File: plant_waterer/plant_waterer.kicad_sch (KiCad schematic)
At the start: 16 parts, among them J1 PJ-002AH, J2 Conn_01x02, J3 Conn_01x03, U1 XIAO_RP2040, U2 TB6612FNG,C,8,EL, U3 OLED_DISP, U4 AP2204R-5.0TRG1

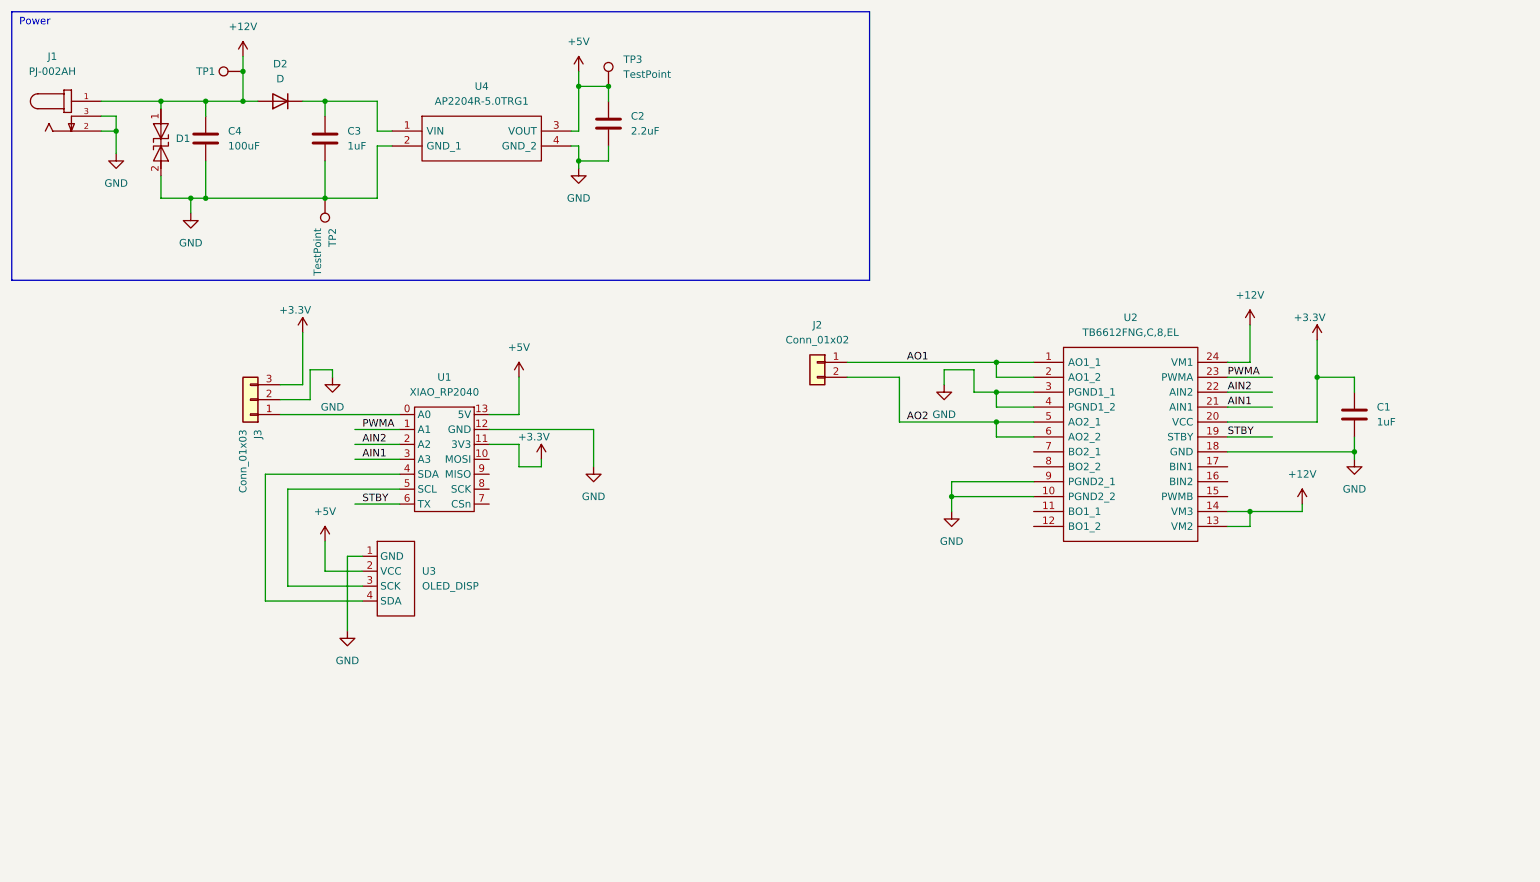
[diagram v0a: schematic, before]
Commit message: Added UART input Added second motor output Added fuse and reverse polarity protection
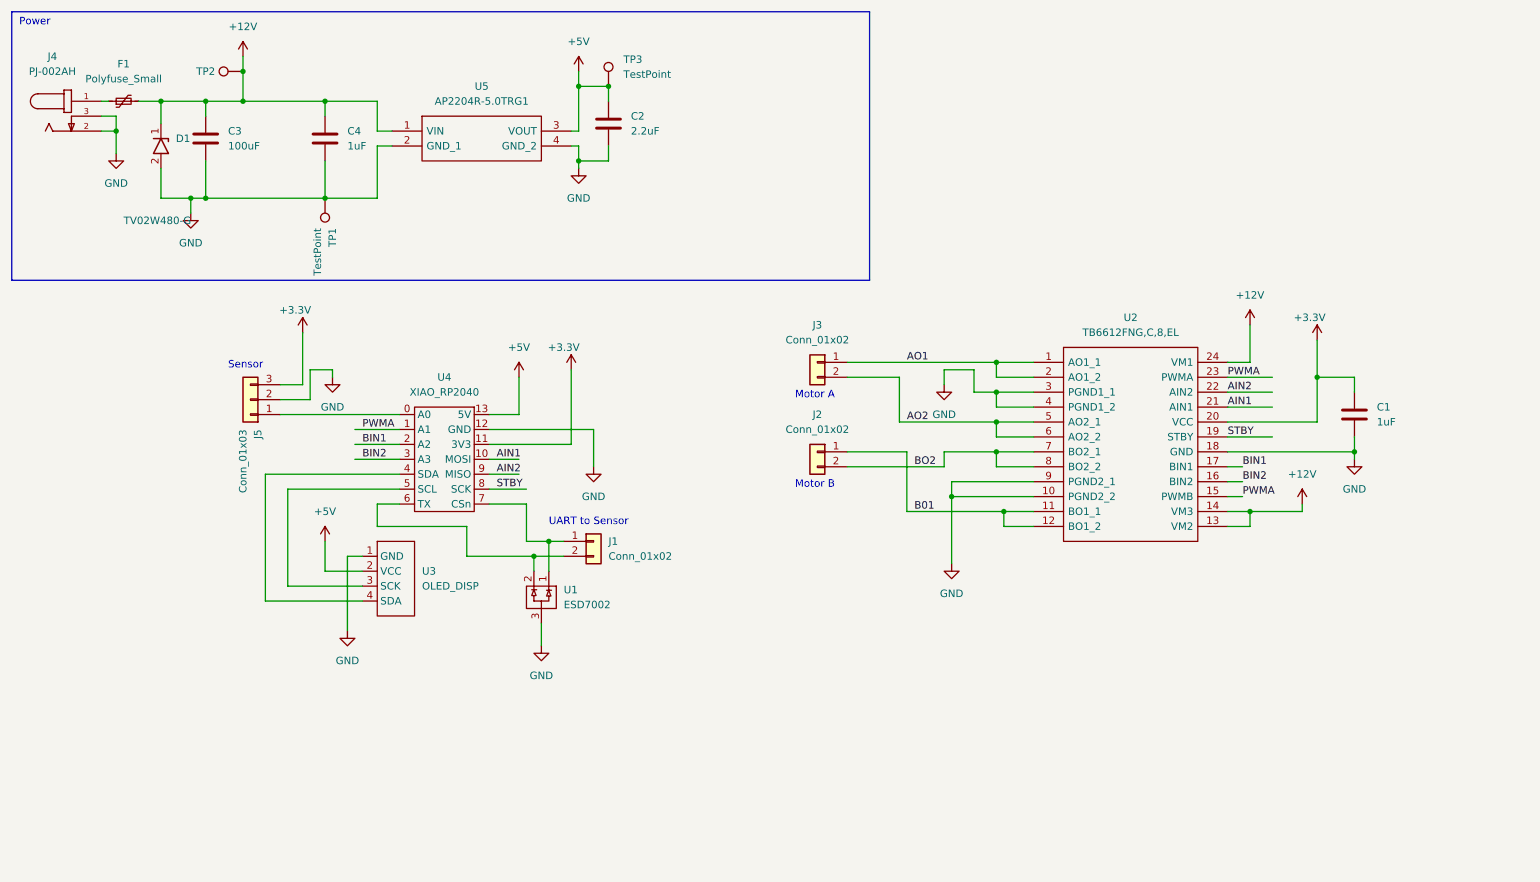
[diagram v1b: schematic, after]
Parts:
- removed D1: SP3130-01ETG, Library:SP3130-01ETG, symbol MySymbols:SP3130-01ETG
- removed D2: D, Diode_SMD:D_SOD-123, symbol Device:D
- added D1: TV02W480-G, Diode_SMD:D_SOD-123, symbol MySymbols:TV02W480-G
- added F1: Polyfuse_Small, Fuse:Fuse_1210_3225Metric_Pad1.42x2.65mm_HandSolder, symbol Device:Polyfuse_Small
- added J1: Conn_01x02, Connector_PinHeader_2.54mm:PinHeader_1x02_P2.54mm_Vertical, symbol Connector_Generic:Conn_01x02
- added J2: Conn_01x02, Library:CONN 1x2 5mm, symbol Connector_Generic:Conn_01x02
- added U1: ESD7002, Package_TO_SOT_SMD:SOT-323_SC-70_Handsoldering, symbol MySymbols:ESD7002
- TP1: renamed from TP2; footprint TestPoint:TestPoint_2Pads_Pitch2.54mm_Drill0.8mm -> TestPoint:TestPoint_Loop_D1.80mm_Drill1.0mm_Beaded
- TP2: renamed from TP1; footprint TestPoint:TestPoint_Pad_1.5x1.5mm -> TestPoint:TestPoint_Loop_D1.80mm_Drill1.0mm_Beaded
- TP3: footprint TestPoint:TestPoint_Pad_1.5x1.5mm -> TestPoint:TestPoint_Loop_D1.80mm_Drill1.0mm_Beaded
- renumbered C4 to C3, C3 to C4, J2 to J3, J1 to J4, J3 to J5, U1 to U4, U4 to U5
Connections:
- net +12V: now also C4.2, U5.1 (VIN), D1.1, F1.2; no longer J4.1
- net AIN1: now also U4.10 (MOSI); no longer U4.3 (A3)
- net AIN2: now also U4.9 (MISO); no longer U4.2 (A2)
- net GND: now also D1.2, U1.3
- net PWMA: now also U2.15 (PWMB)
- net STBY: now also U4.8 (SCK); no longer U4.6 (TX)
- net B01: now reaches U2.11 (BO1_1)
- net B01: now also U2.12 (BO1_2), J2.1 (Pin_1)
- net BIN2: now reaches U2.16 (BIN2)
- net BIN2: now also U4.3 (A3)
- net BIN1: now reaches U2.17 (BIN1)
- net BIN1: now also U4.2 (A2)
- net BO2: now reaches U2.7 (BO2_1)
- net BO2: now also U2.8 (BO2_2), J2.2 (Pin_2)
- net at U4.7 (CSn): now also J1.1 (Pin_1), U1.1
- new net: J1.2 (Pin_2), U1.2, U4.6 (TX)
- new net: F1.1, J4.1
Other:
- note added: "Motor A"
- note added: "Motor B"
- note added: "Sensor"
- note added: "UART to Sensor"

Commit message: Add adjustable level set Add power filtering Add ESD
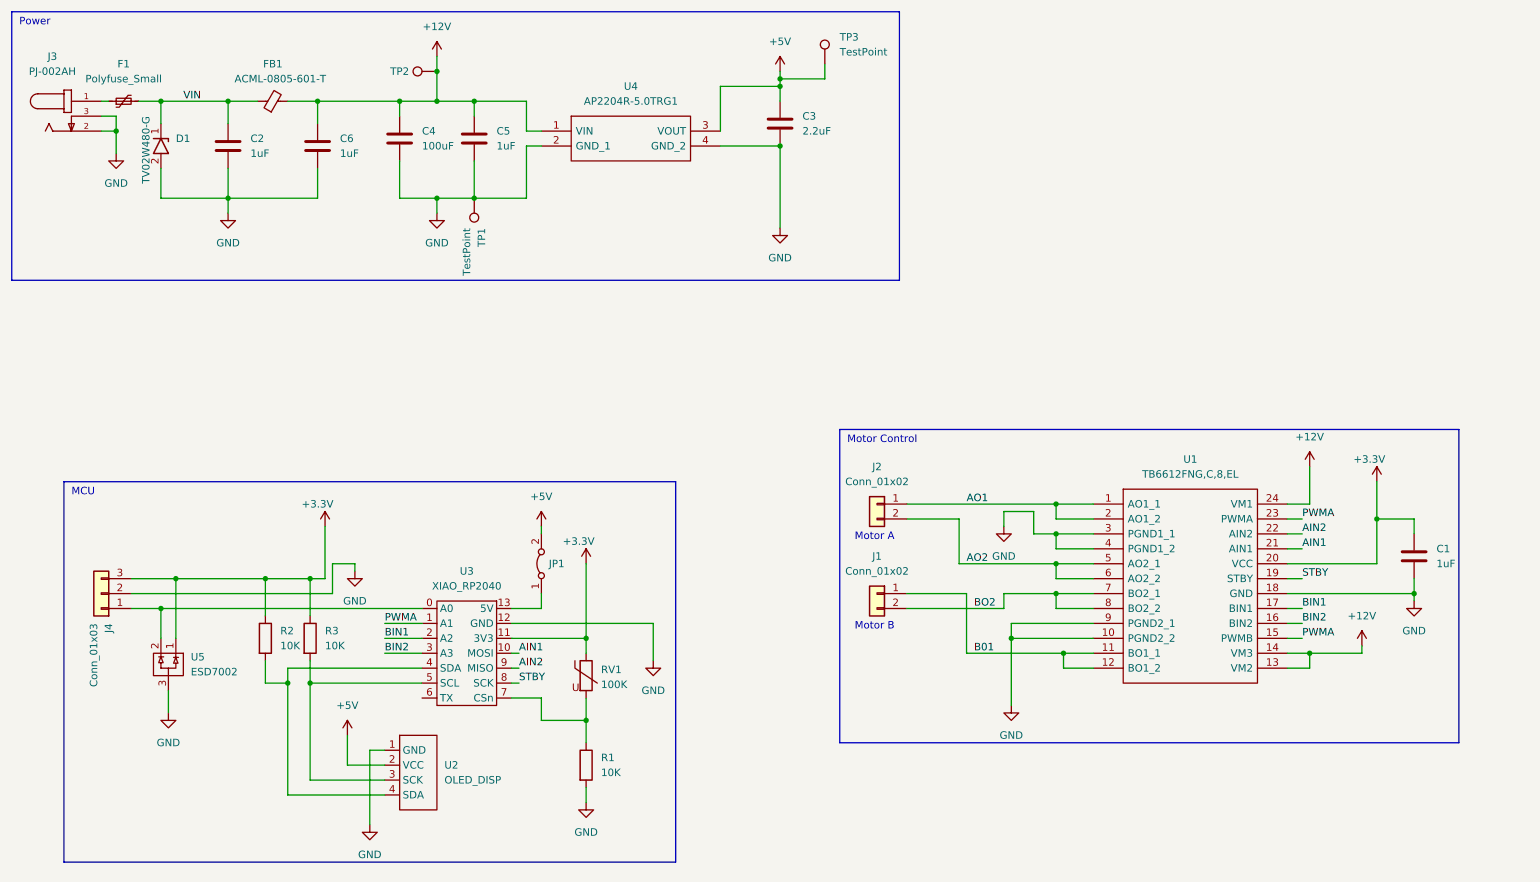
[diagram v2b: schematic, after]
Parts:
- removed J1: Conn_01x02, Connector_PinHeader_2.54mm:PinHeader_1x02_P2.54mm_Vertical, symbol Connector_Generic:Conn_01x02
- removed U1: ESD7002, Package_TO_SOT_SMD:SOT-323_SC-70_Handsoldering, symbol MySymbols:ESD7002
- added C2, C6: 1uF, Capacitor_SMD:C_0805_2012Metric_Pad1.18x1.45mm_HandSolder, symbol Device:C
- added FB1: ACML-0805-601-T, Resistor_SMD:R_0805_2012Metric_Pad1.20x1.40mm_HandSolder, symbol Device:FerriteBead_Small
- added JP1: Jumper_2_Bridged, Connector_PinHeader_2.54mm:PinHeader_1x02_P2.54mm_Vertical, symbol Jumper:Jumper_2_Bridged
- added R1, R2, R3: 10K, Resistor_SMD:R_0805_2012Metric_Pad1.20x1.40mm_HandSolder, symbol Device:R
- added RV1: 100K, Connector_PinHeader_2.54mm:PinHeader_1x03_P2.54mm_Vertical, symbol Device:Varistor
- added U5: ESD7002, Package_TO_SOT_SMD:SOT-323_SC-70_Handsoldering, symbol MySymbols:ESD7002
- renumbered C2 to C3, C3 to C4, C4 to C5, J2 to J1, J3 to J2, J4 to J3, J5 to J4, U2 to U1, U3 to U2, U4 to U3, U5 to U4
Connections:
- net +12V: now also C6.2, FB1.2; no longer D1.1, F1.2
- net +3.3V: now also R2.1, R3.1, RV1.1, U5.1
- net +5V: now also JP1.2 (B); no longer U3.13 (5V)
- net GND: now also C2.1, C6.1, R1.2, U5.3
- net at U3.7 (CSn): now also R1.1, RV1.2
- net at J4.1 (Pin_1), U3.0 (A0): now also U5.2
- net at U2.4 (SDA), U3.4 (SDA): now also R2.2
- net at U2.3 (SCK), U3.5 (SCL): now also R3.2
- new net: JP1.1 (A), U3.13 (5V)
- new net VIN: C2.2, D1.1, F1.2, FB1.1
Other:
- note added: "MCU"
- note added: "Motor Control"
- note removed: "Sensor"
- note removed: "UART to Sensor"
- moved on the sheet: C1, C3, C4, C5, J1, J2, J4, TP1, TP2, TP3, U1, U2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

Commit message: Minor clean up and adding schmatic
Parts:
- renumbered C3 to C2, C2 to C3, U5 to U4, U4 to U5
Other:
- moved on the sheet: TP3
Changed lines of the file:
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@@
   (junction (at 256.54 115.57) (diameter 0) (color 0 0 0 0)
   )
-  (junction (at 148.59 27.94) (diameter 0) (color 0 0 0 0)
-  )
   (junction (at 195.58 115.57) (diameter 0) (color 0 0 0 0)
   )
@@
   (junction (at 54.61 48.26) (diameter 0) (color 0 0 0 0)
   )
+  (junction (at 138.43 29.21) (diameter 0) (color 0 0 0 0)
+  )
   (junction (at 64.77 130.81) (diameter 0) (color 0 0 0 0)
   )
@@
     (stroke (width 0) (type default) (color 0 0 0 0))
   )
-  (polyline (pts (xy 168.91 62.23) (xy 17.78 62.23))
+  (polyline (pts (xy 160.02 62.23) (xy 17.78 62.23))
     (stroke (width 0) (type default) (color 0 0 0 0))
   )
@@
     (stroke (width 0) (type default) (color 0 0 0 0))
   )
-  (wire (pts (xy 148.59 26.67) (xy 148.59 27.94))
-    (stroke (width 0) (type default) (color 0 0 0 0))
-  )
   (wire (pts (xy 105.41 36.83) (xy 107.95 36.83))
     (stroke (width 0) (type default) (color 0 0 0 0))
@@
     (stroke (width 0) (type default) (color 0 0 0 0))
   )
+  (wire (pts (xy 138.43 25.4) (xy 138.43 29.21))
+    (stroke (width 0) (type default) (color 0 0 0 0))
+  )
   (wire (pts (xy 54.61 43.18) (xy 54.61 48.26))
     (stroke (width 0) (type default) (color 0 0 0 0))
@@
     (stroke (width 0) (type default) (color 0 0 0 0))
   )
-  (wire (pts (xy 156.21 27.94) (xy 148.59 27.94))
-    (stroke (width 0) (type default) (color 0 0 0 0))
-  )
   (polyline (pts (xy 26.67 161.29) (xy 130.81 161.29))
     (stroke (width 0) (type default) (color 0 0 0 0))
@@
     (stroke (width 0) (type default) (color 0 0 0 0))
   )
-  (wire (pts (xy 148.59 27.94) (xy 148.59 29.21))
+  (wire (pts (xy 148.59 26.67) (xy 148.59 29.21))
     (stroke (width 0) (type default) (color 0 0 0 0))
   )
@@
     (stroke (width 0) (type default) (color 0 0 0 0))
   )
-  (polyline (pts (xy 168.91 16.51) (xy 168.91 62.23))
+  (polyline (pts (xy 160.02 16.51) (xy 160.02 62.23))
     (stroke (width 0) (type default) (color 0 0 0 0))
   )
@@
     (stroke (width 0) (type default) (color 0 0 0 0))
   )
-  (polyline (pts (xy 17.78 16.51) (xy 168.91 16.51))
+  (polyline (pts (xy 17.78 16.51) (xy 160.02 16.51))
     (stroke (width 0) (type default) (color 0 0 0 0))
   )
@@
   )
   (wire (pts (xy 201.93 125.73) (xy 196.85 125.73))
-    (stroke (width 0) (type default) (color 0 0 0 0))
-  )
-  (wire (pts (xy 156.21 25.4) (xy 156.21 27.94))
     (stroke (width 0) (type default) (color 0 0 0 0))
   )
@@
   (symbol (lib_id "Connector:TestPoint") (at 96.52 48.26 180) (unit 1)
     (in_bom yes) (on_board yes)
-    (property "Reference" "TP1" (id 0) (at 97.7901 53.34 90)
+    (property "Reference" "TP1" (id 0) (at 98.2784 54.5485 0)
       (effects (font (size 1.27 1.27)) (justify left))
     )
     (property "Value" "TestPoint" (id 1) (at 95.25 53.34 90)
-      (effects (font (size 1.27 1.27)) (justify left))
+      (effects (font (size 1.27 1.27)) (justify left) hide)
     )
     (property "Footprint" "TestPoint:TestPoint_Loop_D1.80mm_Drill1.0mm_Beaded" (id 2) (at 91.44 48.26 0)
@@
   (symbol (lib_id "MySymbols:ESD7002") (at 46.99 125.73 270) (unit 1)
     (in_bom yes) (on_board yes) (fields_autoplaced)
-    (property "Reference" "U5" (id 0) (at 48.26 126.3649 90)
+    (property "Reference" "U4" (id 0) (at 48.26 126.3649 90)
       (effects (font (size 1.27 1.27)) (justify left))
     )
@@
   (symbol (lib_id "Device:C") (at 148.59 35.56 180) (unit 1)
     (in_bom yes) (on_board yes)
-    (property "Reference" "C3" (id 0) (at 152.4 34.29 0)
+    (property "Reference" "C2" (id 0) (at 152.4 34.29 0)
       (effects (font (size 1.27 1.27)) (justify right))
     )
@@
   (symbol (lib_id "Device:C") (at 54.61 39.37 180) (unit 1)
     (in_bom yes) (on_board yes)
-    (property "Reference" "C2" (id 0) (at 58.42 38.1 0)
+    (property "Reference" "C3" (id 0) (at 58.42 38.1 0)
       (effects (font (size 1.27 1.27)) (justify right))
     )
@@
   (symbol (lib_id "MySymbols:AP2204R-5.0TRG1") (at 107.95 36.83 0) (unit 1)
     (in_bom yes) (on_board yes) (fields_autoplaced)
-    (property "Reference" "U4" (id 0) (at 123.19 29.21 0))
+    (property "Reference" "U5" (id 0) (at 123.19 29.21 0))
     (property "Value" "AP2204R-5.0TRG1" (id 1) (at 123.19 31.75 0))
     (property "Footprint" "Library:AP2204R50TRG1" (id 2) (at 134.62 34.29 0)
@@
     (pin "1")
   )
-  (symbol (lib_id "Connector:TestPoint") (at 156.21 25.4 0) (unit 1)
-    (in_bom yes) (on_board yes) (fields_autoplaced)
-    (property "Reference" "TP3" (id 0) (at 158.75 20.8279 0)
-      (effects (font (size 1.27 1.27)) (justify left))
-    )
-    (property "Value" "TestPoint" (id 1) (at 158.75 23.3679 0)
-      (effects (font (size 1.27 1.27)) (justify left))
-    )
-    (property "Footprint" "TestPoint:TestPoint_Loop_D1.80mm_Drill1.0mm_Beaded" (id 2) (at 161.29 25.4 0)
-      (effects (font (size 1.27 1.27)) hide)
-    )
-    (property "Datasheet" "~" (id 3) (at 161.29 25.4 0)
+  (symbol (lib_id "Connector:TestPoint") (at 138.43 25.4 0) (unit 1)
+    (in_bom yes) (on_board yes)
+    (property "Reference" "TP3" (id 0) (at 139.7 21.59 0)
+      (effects (font (size 1.27 1.27)) (justify left))
+    )
+    (property "Value" "TestPoint" (id 1) (at 140.97 23.3679 0)
+      (effects (font (size 1.27 1.27)) (justify left) hide)
+    )
+    (property "Footprint" "TestPoint:TestPoint_Loop_D1.80mm_Drill1.0mm_Beaded" (id 2) (at 143.51 25.4 0)
+      (effects (font (size 1.27 1.27)) hide)
+    )
+    (property "Datasheet" "~" (id 3) (at 143.51 25.4 0)
       (effects (font (size 1.27 1.27)) hide)
     )
@@
       (reference "C1") (unit 1) (value "1uF") (footprint "Capacitor_SMD:C_0805_2012Metric_Pad1.18x1.45mm_HandSolder")
     )
+    (path "/b9c55c43-dab5-46ce-966b-43f725d0c1fc"
+      (reference "C2") (unit 1) (value "2.2uF") (footprint "Capacitor_SMD:C_0805_2012Metric_Pad1.18x1.45mm_HandSolder")
+    )
     (path "/c06ac0b3-fcfd-4585-89e5-5630d72080db"
-      (reference "C2") (unit 1) (value "1uF") (footprint "Capacitor_SMD:C_0805_2012Metric_Pad1.18x1.45mm_HandSolder")
-    )
-    (path "/b9c55c43-dab5-46ce-966b-43f725d0c1fc"
-      (reference "C3") (unit 1) (value "2.2uF") (footprint "Capacitor_SMD:C_0805_2012Metric_Pad1.18x1.45mm_HandSolder")
+      (reference "C3") (unit 1) (value "1uF") (footprint "Capacitor_SMD:C_0805_2012Metric_Pad1.18x1.45mm_HandSolder")
     )
     (path "/3f8e828c-b166-4539-94d5-3447548098f5"
@@
       (reference "U3") (unit 1) (value "XIAO_RP2040") (footprint "Library:XIAO RP2040")
     )
+    (path "/468b7f2a-2822-4d54-b87c-c618f015aeee"
+      (reference "U4") (unit 1) (value "ESD7002") (footprint "Package_TO_SOT_SMD:SOT-323_SC-70_Handsoldering")
+    )
     (path "/ee1ff09d-9bad-453d-a6ef-43957c3f1608"
-      (reference "U4") (unit 1) (value "AP2204R-5.0TRG1") (footprint "Library:AP2204R50TRG1")
-    )
-    (path "/468b7f2a-2822-4d54-b87c-c618f015aeee"
-      (reference "U5") (unit 1) (value "ESD7002") (footprint "Package_TO_SOT_SMD:SOT-323_SC-70_Handsoldering")
-    )
-  )
+      (reference "U5") (unit 1) (value "AP2204R-5.0TRG1") (footprint "Library:AP2204R50TRG1")
+    )
+  )
